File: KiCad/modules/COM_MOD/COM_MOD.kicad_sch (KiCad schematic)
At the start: 14 parts, among them J1 Conn_01x01_Pin, J10 XF2J-1824-12A, J2 Conn_01x01_Pin, J3 Conn_01x01_Pin, J4 XF2J-1824-12A, J5 Conn_01x01_Pin, J6 Conn_01x01_Pin, J7 Conn_01x01_Pin, J8 Conn_01x01_Pin, J9 Conn_01x01_Pin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

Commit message: some cleaning + edge plating dry electrode
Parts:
- added J11, J12, J13, J14: Conn_01x01_Pin, Connector_PinHeader_1.27mm:PinHeader_1x01_P1.27mm_Vertical, symbol Connector:Conn_01x01_Pin
- added LED2: WS2812-2020, 00_custom-footprints:WS2812-2020, symbol custom:WS2812-2020
- J10, J4: footprint 00_custom-footprints:XF2J-1824-12A -> Connector_FFC-FPC:XUNPU_FPC_05F_18P_H20
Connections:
- net +3.3V: now also LED2.4 (VDD)
- net GND: now also LED2.2 (GND)
- net LED_IN: now also LED2.3 (DI)
- net LED_OUT: now also LED2.1 (DO)

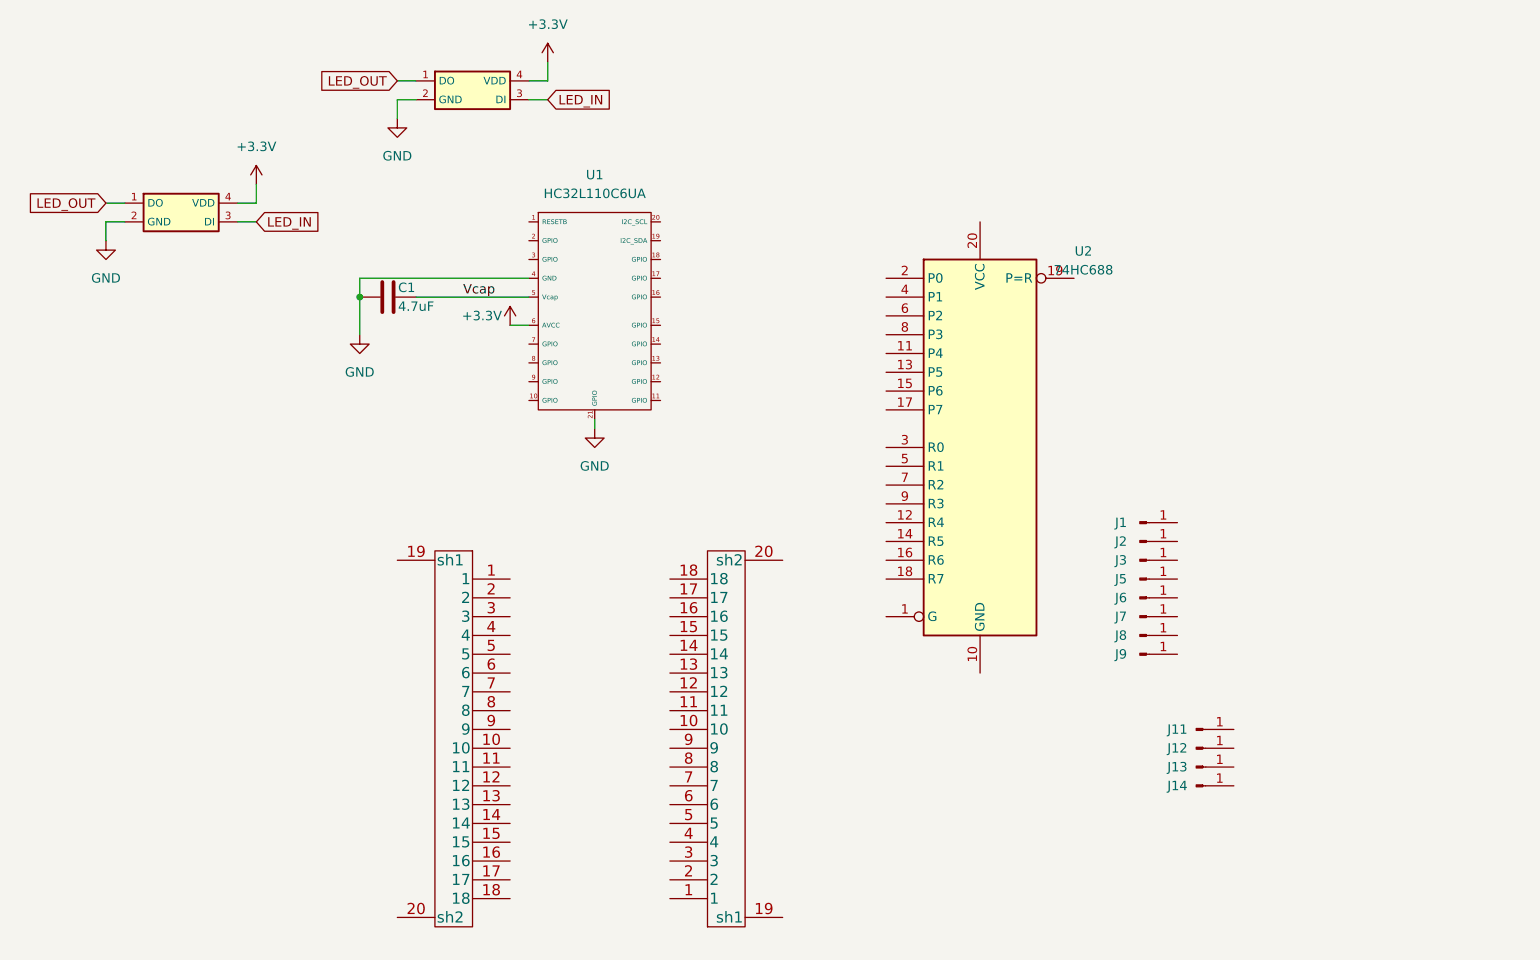
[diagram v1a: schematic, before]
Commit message: finished rooting emgdaq + schematic commod
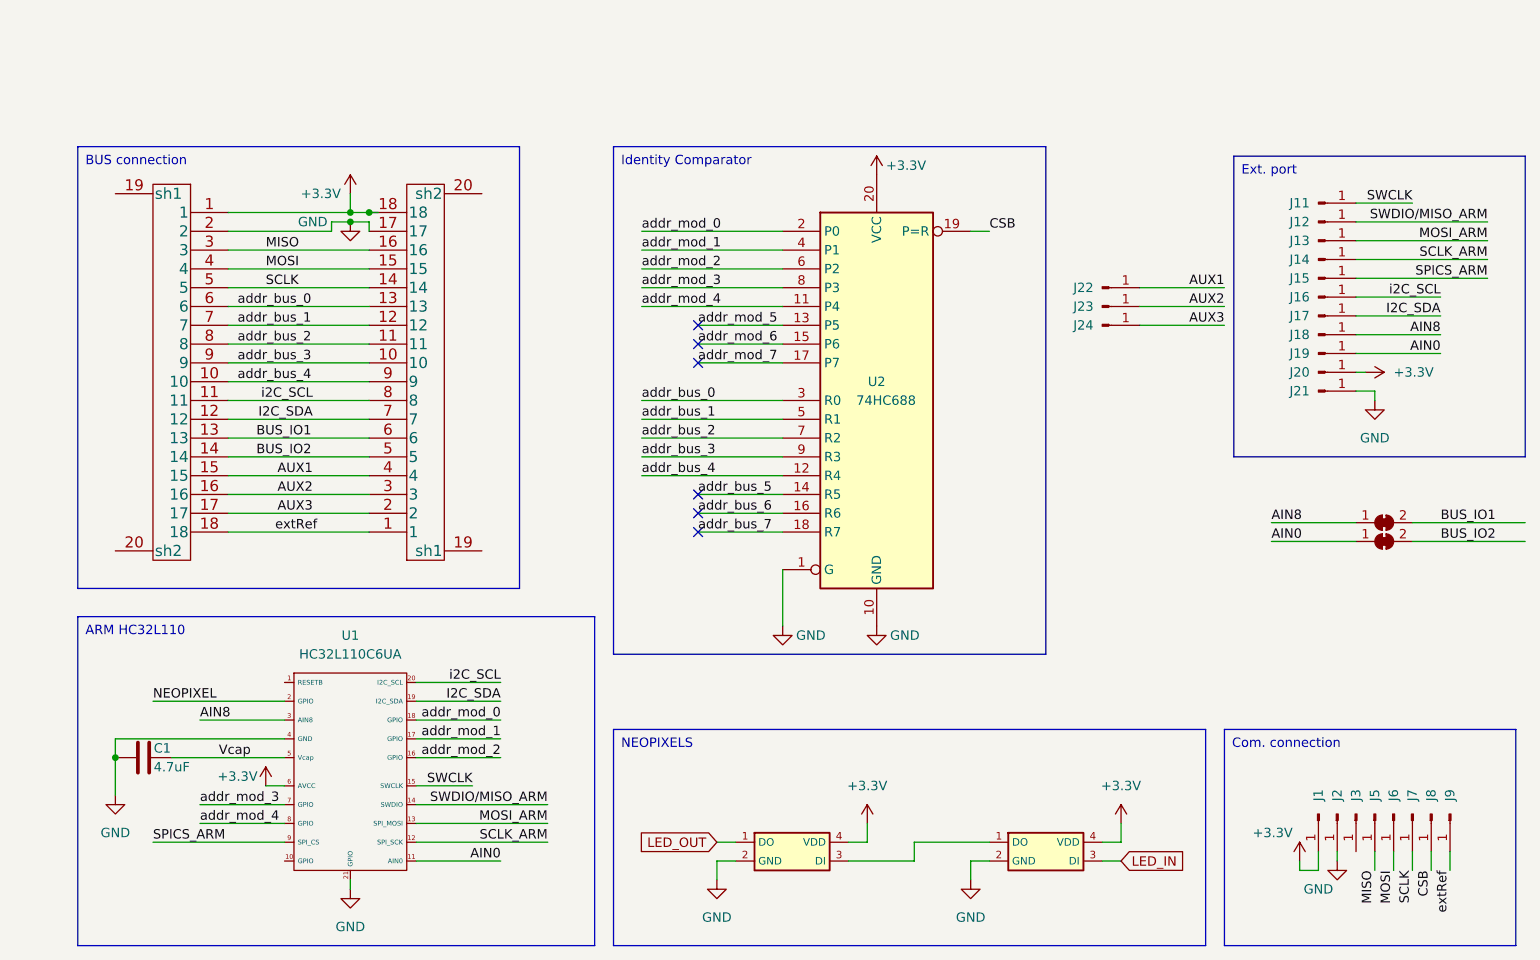
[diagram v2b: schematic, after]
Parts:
- added J15, J16, J17, J18, J19, J20, J21, J22, J23, J24: Conn_01x01_Pin, Connector_PinHeader_1.27mm:PinHeader_1x01_P1.27mm_Vertical, symbol Connector:Conn_01x01_Pin
- added JP1, JP2: SolderJumper_2_Bridged, Jumper:SolderJumper-2_P1.3mm_Bridged_RoundedPad1.0x1.5mm, symbol Jumper:SolderJumper_2_Bridged
- J10, J4: footprint Connector_FFC-FPC:XUNPU_FPC_05F_18P_H20 -> 00_custom-footprints:XUNPU_FPC_05F_18P_H20
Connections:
- net +3.3V: now also J1.1 (Pin_1), J10.18, J4.1, U2.20 (VCC), J20.1 (Pin_1)
- net GND: now also J10.17, J2.1 (Pin_1), J4.2, U2.1 (G), U2.10 (GND), J21.1 (Pin_1)
- net LED_IN: no longer LED2.3 (DI)
- net LED_OUT: no longer LED1.1 (DO)
- net MOSI_ARM: now reaches J13.1 (Pin_1)
- net MOSI_ARM: now also U1.13 (P26)
- net SCLK: now reaches J7.1 (Pin_1)
- net SCLK: now also J10.14, J4.5
- net addr_mod_4: now reaches U2.11 (P4)
- net addr_mod_4: now also U1.8 (P15)
- net addr_bus_4: now reaches U2.12 (R4)
- net addr_bus_4: now also J10.9, J4.10
- net addr_mod_5: now reaches U2.13 (P5)
- net addr_bus_5: now reaches U2.14 (R5)
- net addr_mod_6: now reaches U2.15 (P6)
- net addr_bus_6: now reaches U2.16 (R6)
- net addr_mod_7: now reaches U2.17 (P7)
- net addr_bus_7: now reaches U2.18 (R7)
- net CSB: now reaches U2.19 (P=R)
- net CSB: now also J8.1 (Pin_1)
- net addr_mod_0: now reaches U2.2 (P0)
- net addr_mod_0: now also U1.18 (P34)
- net addr_bus_0: now reaches U2.3 (R0)
- net addr_bus_0: now also J10.13, J4.6
- net addr_mod_1: now reaches U2.4 (P1)
- net addr_mod_1: now also U1.17 (P33)
- net addr_bus_1: now reaches U2.5 (R1)
- net addr_bus_1: now also J10.12, J4.7
- net addr_mod_2: now reaches U2.6 (P2)
- net addr_mod_2: now also U1.16 (P32)
- net addr_bus_2: now reaches U2.7 (R2)
- net addr_bus_2: now also J10.11, J4.8
- net addr_mod_3: now reaches U2.8 (P3)
- net addr_mod_3: now also U1.7 (P03)
- net addr_bus_3: now reaches U2.9 (R3)
- net addr_bus_3: now also J10.10, J4.9
- net AIN0: now reaches U1.11 (P24)
- net AIN0: now also J19.1 (Pin_1), JP2.1 (A)
- net SCLK_ARM: now reaches U1.12 (P25)
- net SCLK_ARM: now also J14.1 (Pin_1)
- net SWDIO/MISO_ARM: now reaches U1.14 (P27)
- net SWDIO/MISO_ARM: now also J12.1 (Pin_1)
- net SWCLK: now reaches U1.15 (P31)
- net SWCLK: now also J11.1 (Pin_1)
- net I2C_SDA: now reaches U1.19 (P35)
- net I2C_SDA: now also J10.7, J4.12, J17.1 (Pin_1)
- net NEOPIXEL: now reaches U1.2 (P01)
- net i2C_SCL: now reaches U1.20 (P36)
- net i2C_SCL: now also J10.8, J4.11, J16.1 (Pin_1)
- net AIN8: now reaches U1.3 (P02)
- net AIN8: now also J18.1 (Pin_1), JP1.1 (A)
- net SPICS_ARM: now reaches U1.9 (P14)
- net SPICS_ARM: now also J15.1 (Pin_1)
- net MOSI: now reaches J6.1 (Pin_1)
- net MOSI: now also J10.15, J4.4
- net extRef: now reaches J9.1 (Pin_1)
- net extRef: now also J10.1, J4.18
- net MISO: now reaches J5.1 (Pin_1)
- net MISO: now also J10.16, J4.3
- net AUX3: now reaches J10.2
- net AUX3: now also J4.17, J24.1 (Pin_1)
- net AUX2: now reaches J10.3
- net AUX2: now also J4.16, J23.1 (Pin_1)
- net AUX1: now reaches J10.4
- net AUX1: now also J4.15, J22.1 (Pin_1)
- net BUS_IO2: now reaches J10.5
- net BUS_IO2: now also J4.14, JP2.2 (B)
- net BUS_IO1: now reaches J10.6
- net BUS_IO1: now also J4.13, JP1.2 (B)
- new net: LED1.1 (DO), LED2.3 (DI)
- no-connect marks 0 -> 6
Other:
- moved on the sheet: C1, J1, J11, J12, J13, J14, J2, J3, J5, J6, J7, J8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

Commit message: lot of updates on ads93,flex,commod,pad
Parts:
- removed J22, J23, J24: Conn_01x01_Pin, Connector_PinHeader_1.27mm:PinHeader_1x01_P1.27mm_Vertical, symbol Connector:Conn_01x01_Pin
- removed JP1, JP2: SolderJumper_2_Bridged, Jumper:SolderJumper-2_P1.3mm_Bridged_RoundedPad1.0x1.5mm, symbol Jumper:SolderJumper_2_Bridged
- added I1: smd_insert, 00_Custom:insert_1.2mm, symbol 00_custom:smd_insert
- added R1: 10K, Resistor_SMD:R_0402_1005Metric, symbol Device:R
- added SW1: NA, 00_Custom:SW-SMD_L3.9-W3.0-P4.45, symbol 00_custom:switch
- C1: LCSC (none) -> C23733
- J10, J4: footprint 00_custom-footprints:XUNPU_FPC_05F_18P_H20 -> 00_Custom:XUNPU_FPC_05F_18P_H20; symbol XF2J-1824-12A:XF2J-1824-12A -> 00_custom:XF2J-1824-12A; LCSC (none) -> C2856802
- LED1, LED2: footprint 00_custom-footprints:WS2812-2020 -> 00_Custom:WS2812-2020; symbol custom:WS2812-2020 -> 00_custom:WS2812-2020
- U1: footprint 00_custom-footprints:QFN-20-1EP_3x3mm_P0.4mm_EP1.4x1.4mm -> 00_Custom:QFN-20-1EP_3x3mm_P0.4mm_EP1.4x1.4mm; symbol XHSC:HC32L110C6UA -> 00_custom:HC32L110C6UA; LCSC (none) -> C493490
- U2: LCSC (none) -> C132045
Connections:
- net NEOPIXEL is gone; now on net LED_IN: U1.2 (P01)
- net SWCLK is gone; now on net IO1_out: J11.1 (Pin_1), U1.15 (P31)
- net addr_bus_5 is gone; now on net GND: U2.14 (R5)
- net addr_bus_6 is gone; now on net GND: U2.16 (R6)
- net addr_bus_7 is gone; now on net GND: U2.18 (R7)
- net addr_mod_5 is gone; now on net GND: U2.13 (P5)
- net addr_mod_6 is gone; now on net GND: U2.15 (P6)
- net addr_mod_7 is gone; now on net GND: U2.17 (P7)
- net +3.3V: now also J10.17, J4.2, R1.1; no longer J10.18, J20.1 (Pin_1), J4.1
- net AIN0: now also J18.1 (Pin_1); no longer J19.1 (Pin_1)
- net AUX1: now also J10.18, J19.1 (Pin_1), J4.1; no longer J10.4, J4.15
- net AUX2: now also J10.2, J20.1 (Pin_1), J4.17; no longer J10.3, J4.16
- net AUX3: now also J10.15, J3.1 (Pin_1), J4.4; no longer J10.2, J4.17
- net GND: now also J10.16, J10.19 (sh1), J10.20 (sh2), J4.19 (sh1), J4.20 (sh2), J4.3, I1.1 (conn), SW1.2; no longer J10.17, J21.1 (Pin_1), J4.2
- net I2C_SDA: now also J10.4, J4.15; no longer J10.7, J4.12
- net MISO: now also J10.9, J4.10; no longer J10.16, J4.3
- net MOSI: now also J10.8, J4.11; no longer J10.15, J4.4
- net SCLK: now also J10.7, J4.12; no longer J10.14, J4.5
- net addr_bus_0: now also J10.14, J4.5; no longer J10.13, J4.6
- net addr_bus_1: now also J10.13, J4.6; no longer J10.12, J4.7
- net addr_bus_2: now also J10.12, J4.7; no longer J10.11, J4.8
- net addr_bus_3: now also J10.11, J4.8; no longer J10.10, J4.9
- net addr_bus_4: now also J10.10, J4.9; no longer J10.9, J4.10
- net i2C_SCL: now also J10.3, J4.16; no longer J10.8, J4.11
- net GPIO: now reaches U1.10 (P23)
- net GPIO: now also J21.1 (Pin_1), R1.2, SW1.1
- net AIN8 renamed IO1_in
- net IO1_in: now also J4.13; no longer J18.1 (Pin_1)
- net BUS_IO1 renamed IO1_out
- net IO1_out: no longer J4.13
- net BUS_IO2 renamed IO2
- no-connect marks 6 -> 0
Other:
- company: (none) -> Aightech
- title: (none) -> CleverHand Communication Module
- moved on the sheet: C1, J1, J11, J12, J13, J14, J15, J16, J17, J18, J2, J3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

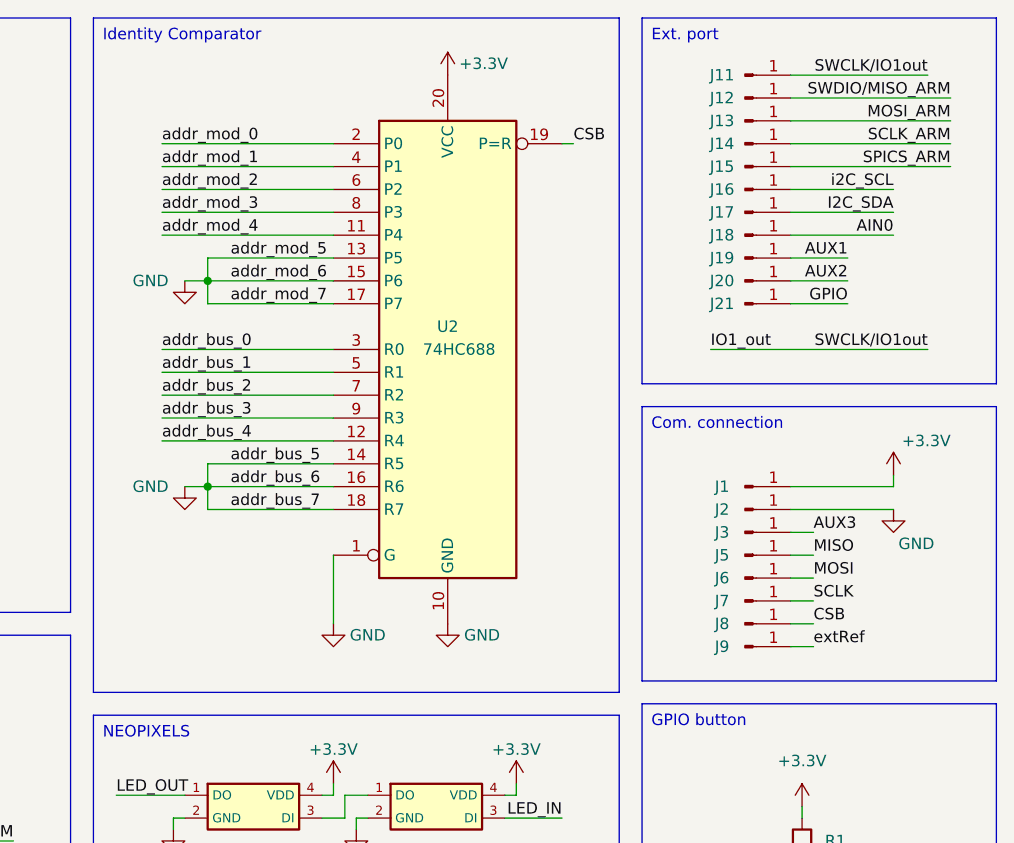
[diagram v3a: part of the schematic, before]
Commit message: finished ads93,commod,drypad,flexpad,jackconn,imubno + plot and render
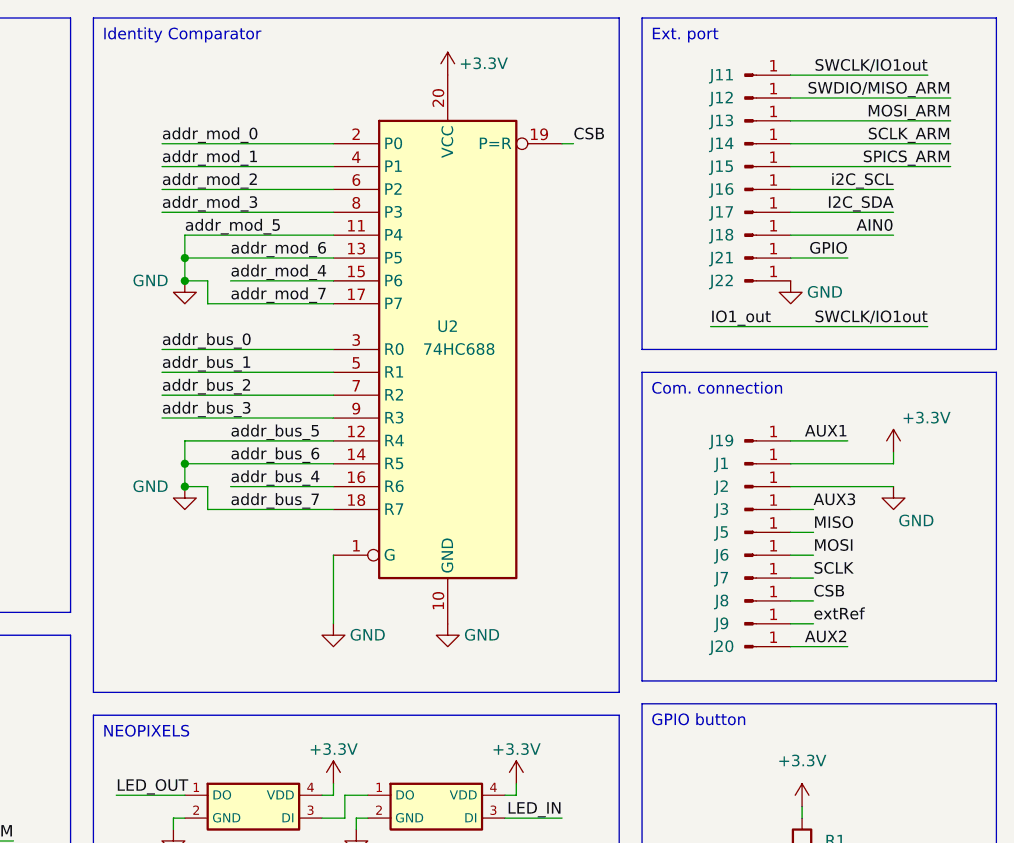
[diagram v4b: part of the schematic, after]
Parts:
- added J22: Conn_01x01_Pin, Connector_PinHeader_1.27mm:PinHeader_1x01_P1.27mm_Vertical, symbol Connector:Conn_01x01_Pin
- LED1, LED2: LCSC (none) -> C2976072
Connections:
- net GND: now also U2.11 (P4), U2.12 (R4), J22.1 (Pin_1); no longer U2.15 (P6), U2.16 (R6)
- net addr_bus_4: now also U2.16 (R6); no longer U2.12 (R4)
- net addr_mod_4: now also U2.15 (P6); no longer U2.11 (P4)
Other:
- moved on the sheet: J1, J19, J2, J20, J21, J3, J5, J6, J7, J8, J9
